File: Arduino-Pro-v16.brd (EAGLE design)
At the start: 100 x 80 mm, 8 parts, among them J1 AVR_SPI_PRG_6NS, U1 ATMEGA328P_TQFP

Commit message: changing the board files
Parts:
- removed C2: 1.0uF, SparkFun-Capacitors:0603-CAP
- removed J1: AVR_SPI_PRG_6NS, SparkFun-Connectors:2X3-NS
- removed J2, J3: (no value), SparkFun-Connectors:1X04
- added C10: 0.1uF, SparkFun:0402-CAP
- added C13: 10uF, SparkFun:EIA3216
- added JP3: ISP, SparkFun:2X3
- added LED1: Red, SparkFun:LED-0603
- added Q1: RESONATORSMD, SparkFun:RESONATOR-SMD
- added R11: 4.7K, SparkFun:0402-RES
- C1, C3: value 1.0uF -> 0.1uF; device SparkFun-Capacitors:0603-CAP -> SparkFun:0402-CAP
- U1: value ATMEGA328P_TQFP -> ATMEGA328; device atmega328pb_tqfn:TQFP32-08 -> SparkFun:TQFP32-08
- moved PCB1 73.6 mm to (-31.8, -57.1)
- moved C3 33.7 mm to (-19.1, 21.6)
- moved C1 25.3 mm to (-15.2, 21.6)
- moved U1 12.7 mm to (-17.8, 7.62)
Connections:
- removed net 3.3V: C1.1, C2.1, C3.1, J2.2, J3.2, U1.18, U1.20, U1.4
- removed net SCL0: J2.4, U1.28
- removed net SCL1: J3.4
- removed net SDA0: J2.3, U1.27
- removed net SDA1: J3.3, U1.3, U1.6
- new net AREF: C1.2, U1.20
- new net MISO: JP3.1
- new net MOSI: JP3.4
- new net N$3: Q1.1, U1.8
- new net N$38: LED1.A, R11.1
- new net N$4: Q1.3, U1.7
- new net RESET: JP3.5
- new net SCK: JP3.3
- new net VCC: C10.1, C13.A, C3.2, JP3.2, R11.2, U1.18, U1.4, U1.6
- net GND: now also C1.1, C10.2, C13.C, C3.1, JP3.6, LED1.C, Q1.2, U1.3; no longer C1.2, C2.2, C3.2, J2.1, J3.1

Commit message: Added the _real_ files for the board
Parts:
- added C2: 0.1uF, SparkFun-Capacitors:0603-CAP
- added C4: (no value), SparkFun-Capacitors:EIA3528
- added J1: (no value), SparkFun-Connectors:1X02
- added LED2: Green, LilyPad-Wearables:LED-1206
- added R1: 1K, SparkFun-Passives:0603-RES
- added R2: 10K, SparkFun-Passives:0603-RES
- added U$1: TACTILE-SWITCH-7914G, GeekAmmo:7914G
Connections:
- net AREF renamed N$6
- new net DTR: C2.1
- new net N$1: LED2.A, R1.1
- net GND: now also C4.C, J1.1, U$1.1, U$1.2
- net MISO: now also U1.16
- net MOSI: now also U1.15
- net RESET: now also C2.2, R2.1, U$1.3, U$1.4, U1.29
- net SCK: now also R1.2, U1.17
- net VCC: now also C4.A, J1.2, R2.2
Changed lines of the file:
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@@
 <?xml version="1.0" encoding="utf-8"?>
 <!DOCTYPE eagle SYSTEM "eagle.dtd">
-<eagle version="7.5.0">
+<eagle version="7.6.0">
 <drawing>
 <settings>
@@
 <layer number="112" name="tSilk" color="7" fill="1" visible="yes" active="yes"/>
 <layer number="113" name="IDFDebug" color="4" fill="1" visible="yes" active="yes"/>
+<layer number="114" name="Badge_Outline" color="7" fill="1" visible="yes" active="yes"/>
+<layer number="115" name="ReferenceISLANDS" color="7" fill="1" visible="yes" active="yes"/>
 <layer number="116" name="Patch_BOT" color="9" fill="4" visible="yes" active="yes"/>
+<layer number="118" name="Rect_Pads" color="7" fill="1" visible="yes" active="yes"/>
 <layer number="121" name="_tsilk" color="7" fill="1" visible="yes" active="yes"/>
 <layer number="122" name="_bsilk" color="7" fill="1" visible="yes" active="yes"/>
@@
 <element name="U1" library="SparkFun" package="TQFP32-08" value="ATMEGA328" x="-17.78" y="7.62"/>
 <element name="PCB1" library="e14_Rpi2_RevA" package="RPI2" value="RPI2" x="-31.75" y="-57.15"/>
+<element name="R1" library="SparkFun-Passives" package="0603-RES" value="1K" x="-30.48" y="-62.23"/>
+<element name="LED2" library="LilyPad-Wearables" package="LED-1206" value="Green" x="-29.21" y="-67.31"/>
+<element name="R2" library="SparkFun-Passives" package="0603-RES" value="10K" x="-30.48" y="-72.39"/>
+<element name="C2" library="SparkFun-Capacitors" package="0603-CAP" value="0.1uF" x="-30.48" y="-76.2"/>
+<element name="U$1" library="GeekAmmo" package="7914G" value="TACTILE-SWITCH-7914G" x="-29.21" y="-83.82"/>
+<element name="J1" library="SparkFun-Connectors" package="1X02" value="" x="-30.48" y="-88.9"/>
+<element name="C4" library="SparkFun-Capacitors" package="EIA3528" value="" x="-36.83" y="-87.63"/>
 </elements>
 <signals>
@@
 <contactref element="U1" pad="21"/>
 <contactref element="U1" pad="3"/>
+<contactref element="U$1" pad="1"/>
+<contactref element="U$1" pad="2"/>
+<contactref element="J1" pad="1"/>
+<contactref element="C4" pad="C"/>
+<wire x1="-30.48" y1="-88.9" x2="-38.48" y2="-87.63" width="0" layer="19" extent="1-1"/>
+<wire x1="-29.21" y1="-83.82" x2="-30.48" y2="-88.9" width="0" layer="19" extent="1-1"/>
+<wire x1="-29.21" y1="-78.3336" x2="-29.21" y2="-83.82" width="0" layer="19" extent="1-1"/>
+<wire x1="-25.4" y1="6.35" x2="-29.21" y2="-78.3336" width="0" layer="19" extent="1-1"/>
 <wire x1="-22.0726" y1="7.22" x2="-25.4" y2="6.35" width="0" layer="19" extent="1-1"/>
 <wire x1="-22.0726" y1="8.82" x2="-22.0726" y2="7.22" width="0" layer="19" extent="1-1"/>
@@
 <wire x1="-13.4874" y1="8.02" x2="-22.0726" y2="7.22" width="0" layer="19" extent="1-1"/>
 </signal>
-<signal name="AREF">
-<contactref element="U1" pad="20"/>
-<contactref element="C1" pad="2"/>
-<wire x1="-14.59" y1="21.59" x2="-13.4874" y2="7.22" width="0" layer="19" extent="1-1"/>
-</signal>
 <signal name="RESET">
 <contactref element="JP3" pad="5"/>
+<contactref element="U1" pad="29"/>
+<contactref element="C2" pad="2"/>
+<contactref element="U$1" pad="3"/>
+<contactref element="U$1" pad="4"/>
+<contactref element="R2" pad="1"/>
+<wire x1="-26.67" y1="-78.3336" x2="-26.67" y2="-83.82" width="0" layer="19" extent="1-1"/>
+<wire x1="-29.63" y1="-76.2" x2="-26.67" y2="-78.3336" width="0" layer="19" extent="1-1"/>
+<wire x1="-31.33" y1="-72.39" x2="-29.63" y2="-76.2" width="0" layer="19" extent="1-1"/>
+<wire x1="-25.4" y1="3.81" x2="-31.33" y2="-72.39" width="0" layer="19" extent="1-1"/>
+<wire x1="-18.18" y1="11.9126" x2="-25.4" y2="3.81" width="0" layer="19" extent="1-1"/>
 </signal>
 <signal name="SCK">
 <contactref element="JP3" pad="3"/>
+<contactref element="U1" pad="17"/>
+<contactref element="R1" pad="2"/>
+<wire x1="-27.94" y1="3.81" x2="-29.63" y2="-62.23" width="0" layer="19" extent="1-1"/>
+<wire x1="-13.4874" y1="4.82" x2="-27.94" y2="3.81" width="0" layer="19" extent="1-1"/>
 </signal>
 <signal name="N$38">
@@
 <signal name="MISO">
 <contactref element="JP3" pad="1"/>
+<contactref element="U1" pad="16"/>
+<wire x1="-14.98" y1="3.3274" x2="-30.48" y2="3.81" width="0" layer="19" extent="1-1"/>
 </signal>
 <signal name="MOSI">
 <contactref element="JP3" pad="4"/>
+<contactref element="U1" pad="15"/>
+<wire x1="-15.78" y1="3.3274" x2="-27.94" y2="6.35" width="0" layer="19" extent="1-1"/>
 </signal>
 <signal name="VCC">
@@
 <contactref element="U1" pad="4"/>
 <contactref element="U1" pad="18"/>
+<contactref element="R2" pad="2"/>
+<contactref element="J1" pad="2"/>
+<contactref element="C4" pad="A"/>
+<wire x1="-27.94" y1="-88.9" x2="-35.18" y2="-87.63" width="0" layer="19" extent="1-1"/>
+<wire x1="-29.63" y1="-72.39" x2="-35.18" y2="-87.63" width="0" layer="19" extent="1-1"/>
+<wire x1="-30.48" y1="6.35" x2="-29.63" y2="-72.39" width="0" layer="19" extent="1-1"/>
 <wire x1="-22.0726" y1="6.42" x2="-30.48" y2="6.35" width="0" layer="19" extent="1-1"/>
 <wire x1="-22.0726" y1="8.02" x2="-22.0726" y2="6.42" width="0" layer="19" extent="1-1"/>
@@
 <wire x1="-22.93" y1="16.51" x2="-22.0726" y2="5.62" width="0" layer="19" extent="1-1"/>
 </signal>
+<signal name="N$1">
+<contactref element="R1" pad="1"/>
+<contactref element="LED2" pad="A"/>
+<wire x1="-31.33" y1="-62.23" x2="-30.71" y2="-67.31" width="0" layer="19" extent="1-1"/>
+</signal>
+<signal name="N$6">
+<contactref element="C1" pad="2"/>
+<contactref element="U1" pad="20"/>
+<wire x1="-13.4874" y1="7.22" x2="-14.59" y2="21.59" width="0" layer="19" extent="1-1"/>
+</signal>
+<signal name="DTR">
+<contactref element="C2" pad="1"/>
+</signal>
 </signals>

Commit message: working on schematic
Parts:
- removed C4: (no value), SparkFun-Capacitors:EIA3528
- removed J1: (no value), SparkFun-Connectors:1X02
- removed Q1: RESONATORSMD, SparkFun:RESONATOR-SMD
- removed U$1: TACTILE-SWITCH-7914G, GeekAmmo:7914G
- removed U1: ATMEGA328, SparkFun:TQFP32-08
- added C5: 0.1uF, SparkFun:0402-CAP
- added C6: 0.1uF, SparkFun-Capacitors:0603-CAP
- added D1: (no value), DiscreteComponents:DO-214AC
- added FRAME1: FRAME-LETTER, SparkFun-Aesthetics:CREATIVE_COMMONS
- added I2C_PIN, SPI_PIN: (no value), SparkFun-Connectors:1X05
- added IC1: ATMEGA1281-16AU, atmel-2005:TQFP64
- added LED3: Yellow, SparkFun:LED-0603
- added LED4: Blue, SparkFun:LED-0603
- added LED5: Red, SparkFun:LED-0603
- added PWM1, PWM2, PWM3: (no value), SparkFun-Connectors:1X04
- added R13, R14, R15, R16, R8, R9: 10K, SparkFun:0402-RES
- added R3: 10K, SparkFun-Passives:0603-RES
- added R4, R5: 220, SparkFun:0402-RES
- added SERIAL1, SERIAL2: (no value), SparkFun-Connectors:1X03
- added T1: (no value), DiscreteComponents:SOT-23
- added U$2: TACTILE-SWITCH-7914G, GeekAmmo:7914G
- added U$3, U$4, U$6: BSS138, DiscreteComponents:SOT-23-BSS138
- added Y1: (no value), SparkFun-FreqCtrl:HC49US
- C1: value 0.1uF -> (none); device SparkFun:0402-CAP -> SparkFun-Capacitors:0603-CAP
- C2: value 0.1uF -> (none)
- LED2: device LilyPad-Wearables:LED-1206 -> SparkFun:LED-0603
- R1: value 1K -> 220; device SparkFun-Passives:0603-RES -> SparkFun:0402-RES
- R2: value 10K -> 220; device SparkFun-Passives:0603-RES -> SparkFun:0402-RES
- moved C1 150.4 mm to (-55.9, -123.2)
- moved R1 136.2 mm to (-72.4, -191.8)
- moved R2 130.1 mm to (-72.4, -195.6)
- moved LED2 125.1 mm to (-62.2, -188.0)
- moved C2 55.7 mm to (-55.9, -125.7)
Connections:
- new net 3V3: R13.2, R15.2, R8.2, U$3.1, U$4.1, U$6.1
- new net 3V3CLK: PCB1.P$23, R15.1, U$6.3
- new net 3V3MISO: PCB1.P$21, R8.1, U$3.3
- new net 3V3MOSI: PCB1.P$19, R13.1, U$4.3
- new net 5VCLK: R16.1, U$6.2
- new net 5VMISO: IC1.13, R9.1, U$3.2
- new net 5VMOSI: IC1.12, R14.1, U$4.2
- new net 5VPROGRAMMER: JP3.2, T1.1
- new net 5VROV: D1.A, T1.3
- new net 5VSCK: IC1.11
- new net N$10: IC1.41, LED3.A
- new net N$11: IC1.42, LED2.A
- new net N$12: PWM1.3
- new net N$13: PWM1.4
- new net N$14: LED5.C, R1.2
- new net N$15: LED4.C, R2.2
- new net N$16: LED3.C, R4.2
- new net N$17: PWM2.4
- new net N$18: PWM3.1
- new net N$19: PWM3.2
- new net N$2: SERIAL1.1
- new net N$20: PWM3.3
- new net N$21: PWM3.4
- new net N$22: LED2.C, R5.2
- new net N$5: IC1.39, LED5.A
- new net N$7: C5.2, IC1.62
- new net N$8: SERIAL2.2
- new net N$9: IC1.40, LED4.A
- new net PWM0A: IC1.17, PWM1.1
- new net PWM0B: IC1.1, PWM1.2
- new net PWM1A: IC1.15, PWM2.1
- new net PWM1B: IC1.16, PWM2.2
- new net PWM1C: PWM2.3
- new net PWM2A: IC1.14
- new net PWM3A: IC1.5
- new net PWM3B: IC1.6
- new net PWM3C: IC1.7
- new net SCL: I2C_PIN.3, IC1.25
- new net SDA: I2C_PIN.2, IC1.26
- new net VCCA: PCB1.P$1
- net DTR: now also C6.1; no longer C2.1
- net GND: now also C1.2, C2.2, C5.1, I2C_PIN.4, I2C_PIN.5, IC1.22, IC1.53, IC1.63, R1.1, R2.1, R4.1, R5.1, SERIAL1.3, SERIAL2.3, SPI_PIN.5, U$2.1, U$2.2; no longer C1.1, C4.C, J1.1, Q1.2, U$1.1, U$1.2, U1.21, U1.3, U1.5
- net MISO: now also SPI_PIN.2; no longer U1.16
- net MOSI: now also SPI_PIN.3; no longer U1.15
- net N$1: now also C1.1, IC1.24, Y1.2; no longer LED2.A, R1.1
- net N$3: now also C2.1, IC1.23, Y1.1; no longer Q1.1, U1.8
- net N$4: now also SERIAL1.2; no longer Q1.3, U1.7
- net N$6: now also SERIAL2.1; no longer C1.2, U1.20
- net RESET: now also C6.2, IC1.20, R3.1, U$2.3, U$2.4; no longer C2.2, R2.1, U$1.3, U$1.4, U1.29
- net SCK: now also SPI_PIN.4; no longer R1.2, U1.17
- net VCC: now also D1.C, I2C_PIN.1, IC1.21, IC1.52, IC1.64, R14.2, R16.2, R3.2, R9.2, SPI_PIN.1, T1.2; no longer C4.A, J1.2, JP3.2, R2.2, U1.18, U1.4, U1.6

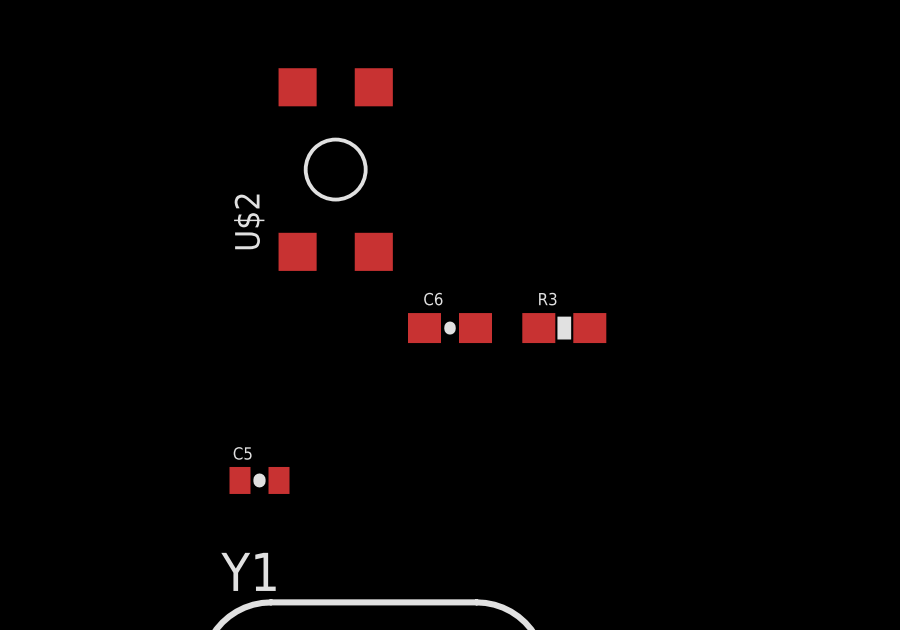
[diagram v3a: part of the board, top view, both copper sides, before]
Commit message: Modified power inputs and added a todo list
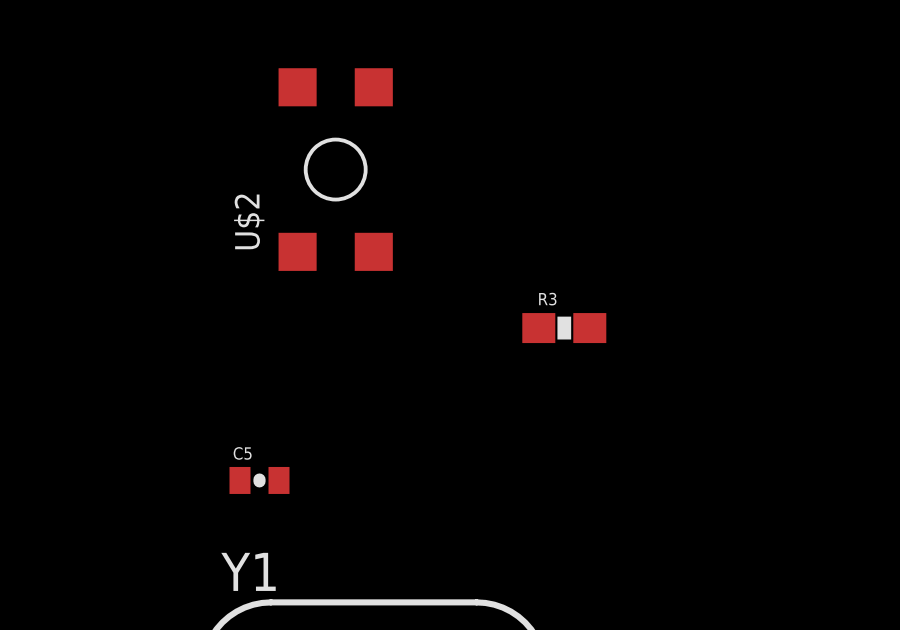
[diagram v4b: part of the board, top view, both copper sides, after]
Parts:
- removed C6: 0.1uF, SparkFun-Capacitors:0603-CAP
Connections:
- removed net DTR: C6.1
- net GND: now also PCB1.P$14, PCB1.P$20, PCB1.P$25, PCB1.P$30, PCB1.P$34, PCB1.P$39, PCB1.P$6, PCB1.P$9
- net RESET: no longer C6.2
- net VCCA: now also PCB1.P$2, PCB1.P$4; no longer PCB1.P$1
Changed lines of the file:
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@@
 <?xml version="1.0" encoding="utf-8"?>
 <!DOCTYPE eagle SYSTEM "eagle.dtd">
-<eagle version="7.6.0">
+<eagle version="7.3.0">
 <drawing>
 <settings>
@@
 <element name="C5" library="SparkFun" package="0402-CAP" value="0.1uF" x="-55.88" y="-113.03"/>
 <element name="R3" library="SparkFun-Passives" package="0603-RES" value="10K" x="-45.72" y="-107.95"/>
-<element name="C6" library="SparkFun-Capacitors" package="0603-CAP" value="0.1uF" x="-49.53" y="-107.95"/>
 <element name="U$2" library="GeekAmmo" package="7914G" value="TACTILE-SWITCH-7914G" x="-54.61" y="-105.41"/>
 <element name="Y1" library="SparkFun-FreqCtrl" package="HC49US" value="" x="-52.07" y="-119.38"/>
@@
 <contactref element="R4" pad="1"/>
 <contactref element="R2" pad="1"/>
+<contactref element="PCB1" pad="P$14"/>
+<contactref element="PCB1" pad="P$20"/>
+<contactref element="PCB1" pad="P$30"/>
+<contactref element="PCB1" pad="P$34"/>
+<contactref element="PCB1" pad="P$6"/>
+<contactref element="PCB1" pad="P$25"/>
+<contactref element="PCB1" pad="P$39"/>
+<contactref element="PCB1" pad="P$9"/>
 <wire x1="-50.8" y1="-161.29" x2="-50.8" y2="-166.37" width="0" layer="19" extent="1-1"/>
 <wire x1="-45.72" y1="-135.89" x2="-50.8" y2="-161.29" width="0" layer="19" extent="1-1"/>
@@
 <wire x1="-73.04" y1="-199.39" x2="-73.04" y2="-195.58" width="0" layer="19" extent="1-1"/>
 <wire x1="-73.04" y1="-203.2" x2="-73.04" y2="-199.39" width="0" layer="19" extent="1-1"/>
-<wire x1="-25.4" y1="6.35" x2="-46.7741" y2="-73.5203" width="0" layer="19" extent="1-1"/>
+<wire x1="-13.2334" y1="-5.9182" x2="-46.7741" y2="-73.5203" width="0" layer="19" extent="1-1"/>
+<wire x1="-18.3134" y1="-3.3782" x2="-13.2334" y2="-5.9182" width="0" layer="19" extent="1-1"/>
+<wire x1="-8.1534" y1="-3.3782" x2="-13.2334" y2="-5.9182" width="0" layer="19" extent="1-1"/>
+<wire x1="-0.5334" y1="-3.3782" x2="-8.1534" y2="-3.3782" width="0" layer="19" extent="1-1"/>
+<wire x1="7.0866" y1="-5.9182" x2="-0.5334" y2="-3.3782" width="0" layer="19" extent="1-1"/>
+<wire x1="12.1666" y1="-3.3782" x2="7.0866" y2="-5.9182" width="0" layer="19" extent="1-1"/>
+<wire x1="17.2466" y1="-3.3782" x2="12.1666" y2="-3.3782" width="0" layer="19" extent="1-1"/>
+<wire x1="24.8666" y1="-5.9182" x2="17.2466" y2="-3.3782" width="0" layer="19" extent="1-1"/>
+<wire x1="-25.4" y1="6.35" x2="-18.3134" y2="-3.3782" width="0" layer="19" extent="1-1"/>
 <wire x1="-30.61" y1="15.24" x2="-25.4" y2="6.35" width="0" layer="19" extent="1-1"/>
 <wire x1="-22.21" y1="21.59" x2="-30.61" y2="15.24" width="0" layer="19" extent="1-1"/>
@@
 <signal name="RESET">
 <contactref element="JP3" pad="5"/>
-<contactref element="C6" pad="2"/>
 <contactref element="U$2" pad="3"/>
 <contactref element="U$2" pad="4"/>
 <contactref element="R3" pad="1"/>
 <contactref element="IC1" pad="20"/>
-<wire x1="-46.57" y1="-107.95" x2="-48.68" y2="-107.95" width="0" layer="19" extent="1-1"/>
-<wire x1="-52.07" y1="-105.41" x2="-48.68" y2="-107.95" width="0" layer="19" extent="1-1"/>
 <wire x1="-52.07" y1="-99.9236" x2="-52.07" y2="-105.41" width="0" layer="19" extent="1-1"/>
+<wire x1="-46.57" y1="-107.95" x2="-52.07" y2="-105.41" width="0" layer="19" extent="1-1"/>
 <wire x1="-53.0733" y1="-89.0397" x2="-52.07" y2="-99.9236" width="0" layer="19" extent="1-1"/>
 <wire x1="-25.4" y1="3.81" x2="-53.0733" y2="-89.0397" width="0" layer="19" extent="1-1"/>
@@
 <wire x1="-18.4" y1="21.59" x2="-23.51" y2="21.59" width="0" layer="19" extent="1-1"/>
 </signal>
-<signal name="DTR">
-<contactref element="C6" pad="1"/>
-</signal>
 <signal name="N$7">
 <contactref element="IC1" pad="62"/>
@@
 <contactref element="R5" pad="2"/>
 <wire x1="-71.74" y1="-203.2" x2="-62.23" y2="-187.21" width="0" layer="19" extent="1-1"/>
-</signal>
-<signal name="VCCA">
-<contactref element="PCB1" pad="P$1"/>
 </signal>
 <signal name="5VMOSI">
@@
 <contactref element="IC1" pad="11"/>
 </signal>
+<signal name="VCCA">
+<contactref element="PCB1" pad="P$2"/>
+<contactref element="PCB1" pad="P$4"/>
+<wire x1="-20.8534" y1="-3.3782" x2="-23.3934" y2="-3.3782" width="0" layer="19" extent="1-1"/>
+</signal>
 </signals>
